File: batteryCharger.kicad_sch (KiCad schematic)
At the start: 7 parts, among them J1 USB4125-GF-A_REVA2, U3 MCP73811T-420I/OT

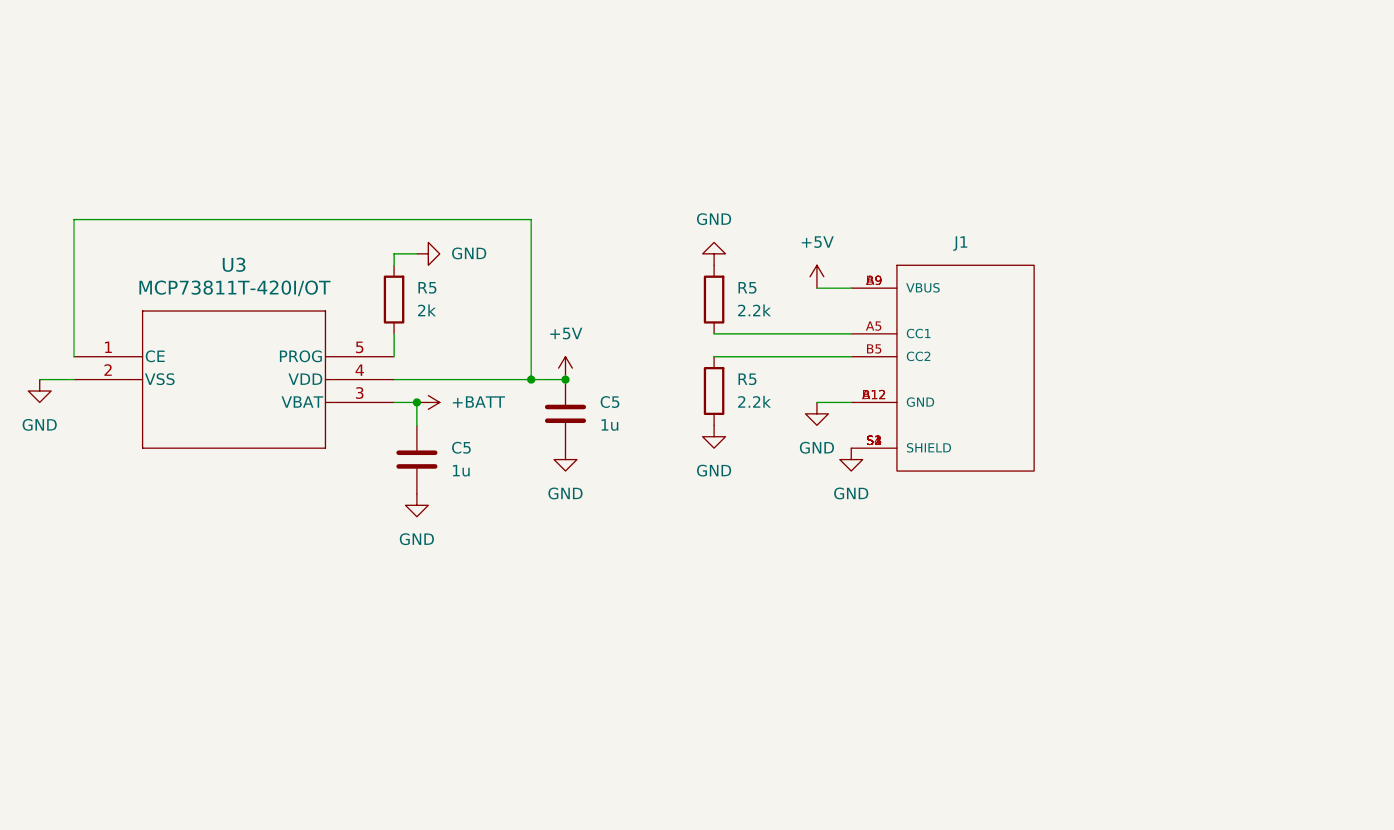
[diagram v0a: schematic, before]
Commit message: version 4: changed GPIO expander, added current sense resistor to electrodes, added buzzer pins, fixed some gpio inputs that needs to be pulled high, added battery charge detection, added battery level measurement feature
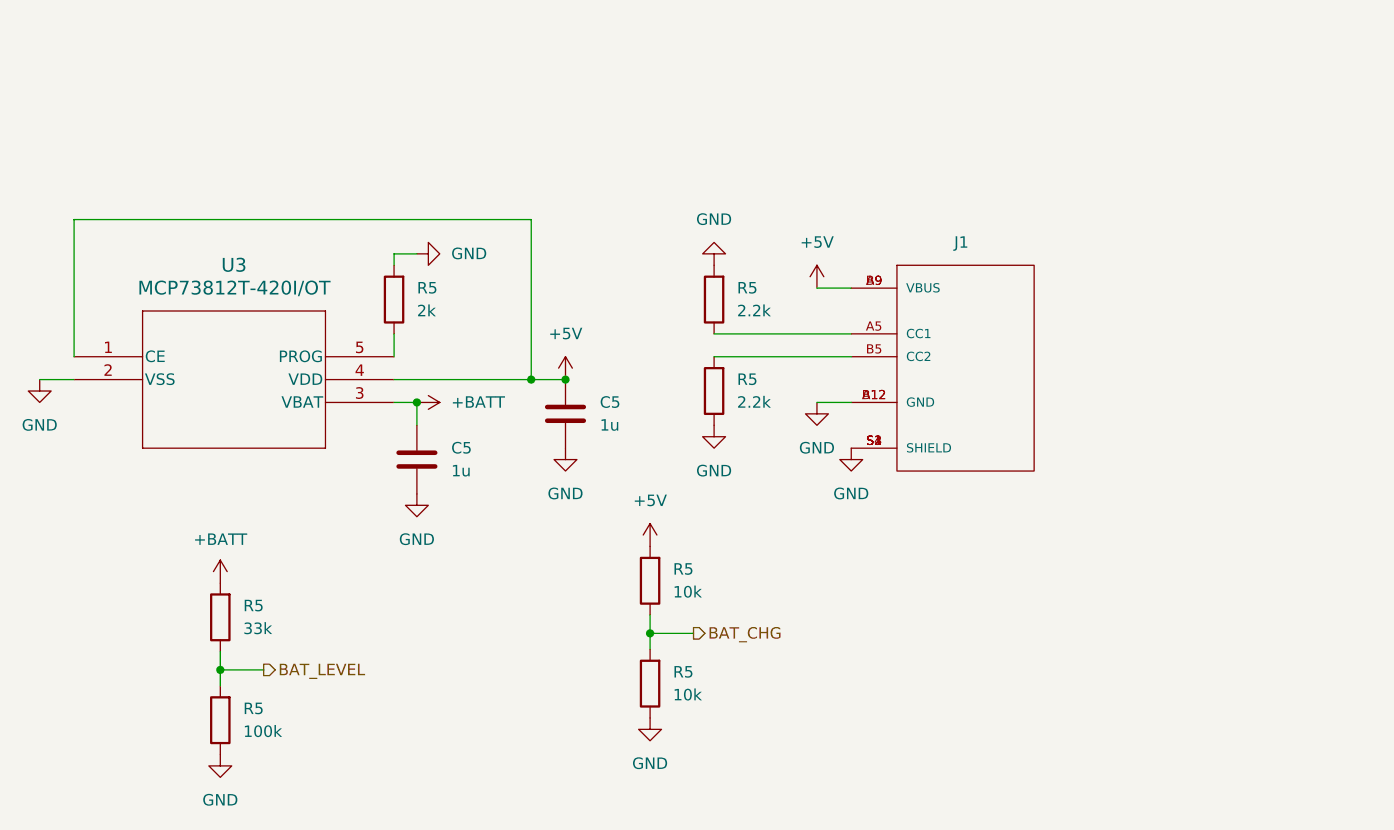
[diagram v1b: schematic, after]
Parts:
- added R5: 100k, Resistor_SMD:R_0402_1005Metric, symbol Device:R
- added R5 (x2): 10k, Resistor_SMD:R_0402_1005Metric, symbol Device:R
- added R5: 33k, Resistor_SMD:R_0402_1005Metric, symbol Device:R
- U3: value MCP73811T-420I/OT -> MCP73812T-420I/OT; Manufacturer Part Number MCP73811T-420I/OT -> MCP73812T-420I/OT
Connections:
- net +5V: now also R5.2
- net +BATT: now also R5.2
- net GND: now also R5.1, R5.1
- new net BAT_CHG: R5.1, R5.2
- new net BAT_LEVEL: R5.1, R5.2

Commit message: version 5: replaced ESP32-WROVER module with ESP-Mini, removed 2.5mm plugs, changed USB connector and routed electrode signals on it, added RC snubber circuit to boost converter and output caps to reduce switching loop
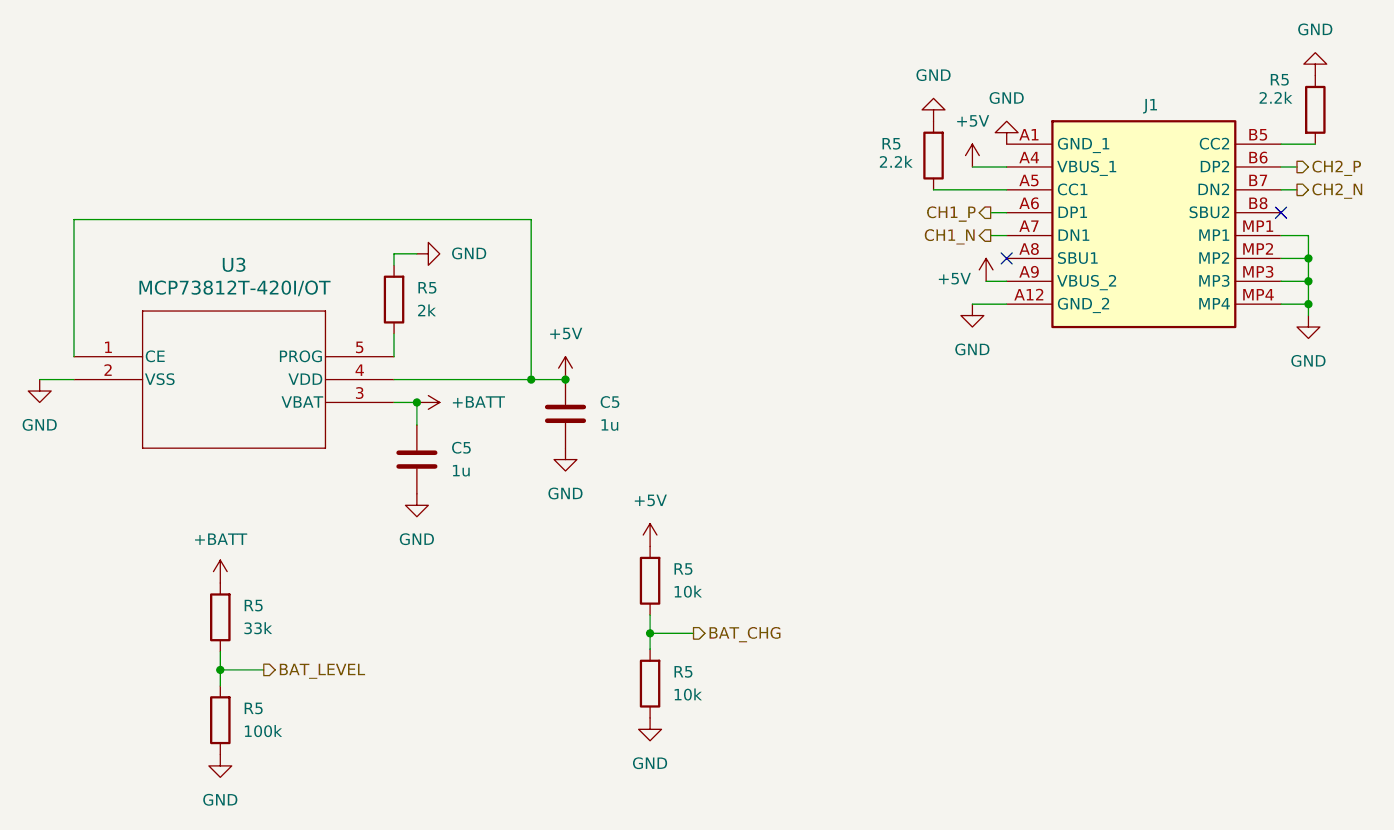
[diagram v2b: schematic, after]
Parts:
- removed J1: USB4125-GF-A_REVA2, Library:GCT_USB4125-GF-A_REVA2, symbol 2023-09-03_14-36-57:USB4125-GF-A_REVA2
- removed R5 (x2): 2.2k, Resistor_SMD:R_0402_1005Metric, symbol Device:R
- added J1: GSB1C41110SSHR, GSB1C41110SSHR, symbol 2023-09-03_14-36-57:GSB1C41110SSHR
- added R5 (x2): 2.2k, Resistor_SMD:R_0402_1005Metric, symbol Device:R
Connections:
- net +5V: now also J1.A4 (VBUS_1), J1.A9 (VBUS_2)
- net GND: now also J1.A1 (GND_1), J1.A12 (GND_2), J1.MP1, J1.MP2, J1.MP3, J1.MP4, R5.1, R5.2
- new net: J1.A5 (CC1), R5.1
- new net: J1.B5 (CC2), R5.2
- new net CH1_N: J1.A7 (DN1)
- new net CH1_P: J1.A6 (DP1)
- new net CH2_N: J1.B7 (DN2)
- new net CH2_P: J1.B6 (DP2)
- no-connect marks 0 -> 2
